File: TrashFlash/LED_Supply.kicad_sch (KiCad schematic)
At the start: 17 parts, among them IC1 LTC3643IUDD#PBF

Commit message: Added Power Supply
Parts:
- R14: value 3.3M -> 560k
- R15: value 68k -> 12k
- R17: value 470k -> 56k
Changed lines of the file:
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@@
 			)
 		)
-		(property "Value" "68k"
+		(property "Value" "12k"
 			(at 160.02 93.9799 0)
 			(effects
@@
 			)
 		)
-		(property "Value" "3.3M"
+		(property "Value" "560k"
 			(at 160.02 69.8499 0)
 			(effects
@@
 			)
 		)
-		(property "Value" "470k"
+		(property "Value" "56k"
 			(at 125.73 83.82 90)
 			(effects

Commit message: Added Battery Management
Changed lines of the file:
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@@
 	)
 	(hierarchical_label "V_LED"
-		(shape input)
+		(shape output)
 		(at 222.25 63.5 0)
 		(effects

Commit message: Added USB and powernets
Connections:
- net V_BAT renamed VSYS
- net V_LED renamed Vdrive
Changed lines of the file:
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@@
+	(wire
+		(pts
+			(xy 55.88 38.1) (xy 93.98 38.1)
+		)
+		(stroke
+			(width 0)
+			(type default)
+		)
+	)
 	(wire
 		(pts
@@
 	(wire
 		(pts
-			(xy 195.58 63.5) (xy 222.25 63.5)
-		)
-		(stroke
-			(width 0)
-			(type default)
-		)
-	)
-	(wire
-		(pts
 			(xy 157.48 87.63) (xy 157.48 88.9)
 		)
@@
 	(wire
 		(pts
-			(xy 54.61 38.1) (xy 93.98 38.1)
-		)
-		(stroke
-			(width 0)
-			(type default)
-		)
-	)
-	(wire
-		(pts
 			(xy 157.48 120.65) (xy 157.48 121.92)
 		)
@@
 	(wire
 		(pts
+			(xy 195.58 59.69) (xy 195.58 63.5)
+		)
+		(stroke
+			(width 0)
+			(type default)
+		)
+	)
+	(wire
+		(pts
 			(xy 93.98 63.5) (xy 93.98 64.77)
 		)
@@
 			(width 0)
 			(type default)
-		)
-	)
-	(hierarchical_label "V_BAT"
-		(shape input)
-		(at 54.61 38.1 180)
-		(effects
-			(font
-				(size 1.27 1.27)
-			)
-			(justify right)
-		)
-	)
-	(hierarchical_label "V_LED"
-		(shape output)
-		(at 222.25 63.5 0)
-		(effects
-			(font
-				(size 1.27 1.27)
-			)
-			(justify left)
 		)
 	)
@@
 	)
 	(symbol
+		(lib_id "TrashFlash:VSYS")
+		(at 55.88 38.1 90)
+		(unit 1)
+		(exclude_from_sim no)
+		(in_bom yes)
+		(on_board yes)
+		(dnp no)
+		(fields_autoplaced yes)
+		(property "Reference" "#PWR051"
+			(at 50.292 27.94 0)
+			(effects
+				(font
+					(size 1.27 1.27)
+				)
+				(hide yes)
+			)
+		)
+		(property "Value" "VSYS"
+			(at 52.07 38.0999 90)
+			(effects
+				(font
+					(size 1.27 1.27)
+				)
+				(justify left)
+			)
+		)
+		(property "Footprint" ""
+			(at 55.88 38.1 0)
+			(effects
+				(font
+					(size 1.27 1.27)
+				)
+				(hide yes)
+			)
+		)
+		(property "Datasheet" ""
+			(at 55.88 38.1 0)
+			(effects
+				(font
+					(size 1.27 1.27)
+				)
+				(hide yes)
+			)
+		)
+		(property "Description" "Power symbol creates a global label with name \"VSYS\""
+			(at 46.482 37.592 0)
+			(effects
+				(font
+					(size 1.27 1.27)
+				)
+				(hide yes)
+			)
+		)
+		(pin "1"
+		)
+		(instances
+			(project ""
+				(path "/256082dc-9c82-41ae-bfb7-0b4bd4121c78/20812885-5a6f-4708-82f0-e6ad3403d690"
+					(reference "#PWR051")
+					(unit 1)
+				)
+			)
+		)
+	)
+	(symbol
 		(lib_id "power:GND")
 		(at 195.58 143.51 0)
@@
 				)
 			)
+		)
+	)
+	(symbol
+		(lib_id "power:Vdrive")
+		(at 195.58 59.69 0)
+		(unit 1)
+		(exclude_from_sim no)
+		(in_bom yes)
+		(on_board yes)
+		(dnp no)
+		(fields_autoplaced yes)
+		(property "Reference" "#PWR050"
+			(at 195.58 63.5 0)
+			(effects
+				(font
+					(size 1.27 1.27)
+				)
+				(hide yes)
+			)
+		)
+		(property "Value" "Vdrive"
+			(at 195.58 54.61 0)
+			(effects
+				(font
+					(size 1.27 1.27)
+				)
+			)
+		)
+		(property "Footprint" ""
+			(at 195.58 59.69 0)
+			(effects
+				(font
+					(size 1.27 1.27)
+				)
+				(hide yes)
+			)
+		)
+		(property "Datasheet" ""
+			(at 195.58 59.69 0)
+			(effects
+				(font
+					(size 1.27 1.27)
+				)
+				(hide yes)
+			)
+		)
+		(property "Description" "Power symbol creates a global label with name \"Vdrive\""
+			(at 195.58 59.69 0)
+			(effects
+				(font
+					(size 1.27 1.27)
+				)
+				(hide yes)
+			)
+		)
+		(pin "1"
+		)
+		(instances
+			(project ""
+				(path "/256082dc-9c82-41ae-bfb7-0b4bd4121c78/20812885-5a6f-4708-82f0-e6ad3403d690"
+					(reference "#PWR050")
+					(unit 1)
+				)
+			)

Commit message: Rotary encoder added + 3D stuff
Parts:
- C10, C6, C9: footprint (none) -> Capacitor_SMD:C_0402_1005Metric
- C11, C5, C7: footprint (none) -> Capacitor_SMD:C_0603_1608Metric
- IC1: footprint QFN50P300X500X80-25N-D -> TrashFlash:QFN50P300X500X80-25N-D
- L1: footprint INDPM5454X310N -> TrashFlash:INDPM5454X310N
- R10: footprint (none) -> Resistor_SMD:R_0603_1608Metric
- R11, R12, R13, R14, R15, R16, R17: footprint (none) -> Resistor_SMD:R_0402_1005Metric
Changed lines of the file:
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@@
 			)
 		)
-		(property "Footprint" ""
+		(property "Footprint" "Resistor_SMD:R_0402_1005Metric"
 			(at 159.258 92.71 90)
 			(effects
@@
 			)
 		)
-		(property "Footprint" ""
+		(property "Footprint" "Resistor_SMD:R_0402_1005Metric"
 			(at 159.258 68.58 90)
 			(effects
@@
 			)
 		)
-		(property "Footprint" ""
+		(property "Footprint" "Capacitor_SMD:C_0402_1005Metric"
 			(at 158.4452 129.54 0)
 			(effects
@@
 			)
 		)
-		(property "Footprint" ""
+		(property "Footprint" "Capacitor_SMD:C_0603_1608Metric"
 			(at 75.8952 36.83 0)
 			(effects
@@
 			)
 		)
-		(property "Footprint" ""
+		(property "Footprint" "Capacitor_SMD:C_0603_1608Metric"
 			(at 196.5452 129.54 0)
 			(effects
@@
 			)
 		)
-		(property "Footprint" ""
+		(property "Footprint" "Resistor_SMD:R_0402_1005Metric"
 			(at 95.758 58.42 90)
 			(effects
@@
 			)
 		)
-		(property "Footprint" ""
+		(property "Footprint" "Resistor_SMD:R_0402_1005Metric"
 			(at 95.758 48.26 90)
 			(effects
@@
 			)
 		)
-		(property "Footprint" ""
+		(property "Footprint" "Capacitor_SMD:C_0603_1608Metric"
 			(at 177.4952 72.39 0)
 			(effects
@@
 			)
 		)
-		(property "Footprint" ""
+		(property "Footprint" "Resistor_SMD:R_0603_1608Metric"
 			(at 95.758 33.02 90)
 			(effects
@@
 			)
 		)
-		(property "Footprint" ""
+		(property "Footprint" "Resistor_SMD:R_0402_1005Metric"
 			(at 125.73 85.852 90)
 			(effects
@@
 			)
 		)
-		(property "Footprint" "QFN50P300X500X80-25N-D"
+		(property "Footprint" "TrashFlash:QFN50P300X500X80-25N-D"
 			(at 113.284 170.434 0)
 			(effects
@@
 			)
 		)
-		(property "Footprint" "INDPM5454X310N"
+		(property "Footprint" "TrashFlash:INDPM5454X310N"
 			(at 173.99 129.21 0)
 			(effects
@@
 			)
 		)
-		(property "Footprint" "QFN50P300X500X80-25N-D"
+		(property "Footprint" "TrashFlash:QFN50P300X500X80-25N-D"
 			(at 113.284 80.264 0)
 			(effects
@@
 			)
 		)
-		(property "Footprint" ""
+		(property "Footprint" "Capacitor_SMD:C_0402_1005Metric"
 			(at 177.4952 129.54 0)
 			(effects
@@
 			)
 		)
-		(property "Footprint" ""
+		(property "Footprint" "Capacitor_SMD:C_0402_1005Metric"
 			(at 158.4452 52.07 0)
 			(effects
@@
 			)
 		)
-		(property "Footprint" ""
+		(property "Footprint" "Resistor_SMD:R_0402_1005Metric"
 			(at 95.758 68.58 90)
 			(effects
@@
 			)
 		)
-		(property "Footprint" ""
+		(property "Footprint" "Resistor_SMD:R_0402_1005Metric"
 			(at 159.258 135.89 90)
 			(effects

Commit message: Footprints 3D model fixed
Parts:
- IC1: footprint TrashFlash:QFN50P300X500X80-25N-D -> QFN50P300X500X80-25N-D
- L1: footprint TrashFlash:INDPM5454X310N -> INDPM5454X310N
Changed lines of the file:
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@@
 	)
 	(symbol
-		(lib_name "LTC3643IUDD#PBF_1")
 		(lib_id "TrashFlash:LTC3643IUDD#PBF")
 		(at 125.73 113.03 0)
@@
 			)
 		)
-		(property "Footprint" "TrashFlash:QFN50P300X500X80-25N-D"
+		(property "Footprint" "QFN50P300X500X80-25N-D"
 			(at 113.284 170.434 0)
 			(effects
@@
 			)
 		)
-		(property "Footprint" "TrashFlash:INDPM5454X310N"
+		(property "Footprint" "INDPM5454X310N"
 			(at 173.99 129.21 0)
 			(effects
@@
 			)
 		)
-		(property "Footprint" "TrashFlash:QFN50P300X500X80-25N-D"
+		(property "Footprint" "QFN50P300X500X80-25N-D"
 			(at 113.284 80.264 0)
 			(effects

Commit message: Added STM32 to schematic
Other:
- note added: "Change this so we can turn on with MCU!"
- note added: "Vdrive range: 16.6 V to 34.6 V"
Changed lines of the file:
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@@
 	(generator_version "9.0")
 	(paper "A4")
+	(text "Vdrive range:\n16.6 V to 34.6 V"
+		(exclude_from_sim no)
+		(at 144.78 85.09 0)
+		(effects
+			(font
+				(face "Consolas")
+				(size 1.27 1.27)
+			)
+		)
+	)
+	(text "Change this so we can turn on with MCU!\n"
+		(exclude_from_sim no)
+		(at 90.678 60.706 90)
+		(effects
+			(font
+				(face "Consolas")
+				(size 1.27 1.27)
+			)
+		)
+	)
 	(junction
 		(at 176.53 63.5)

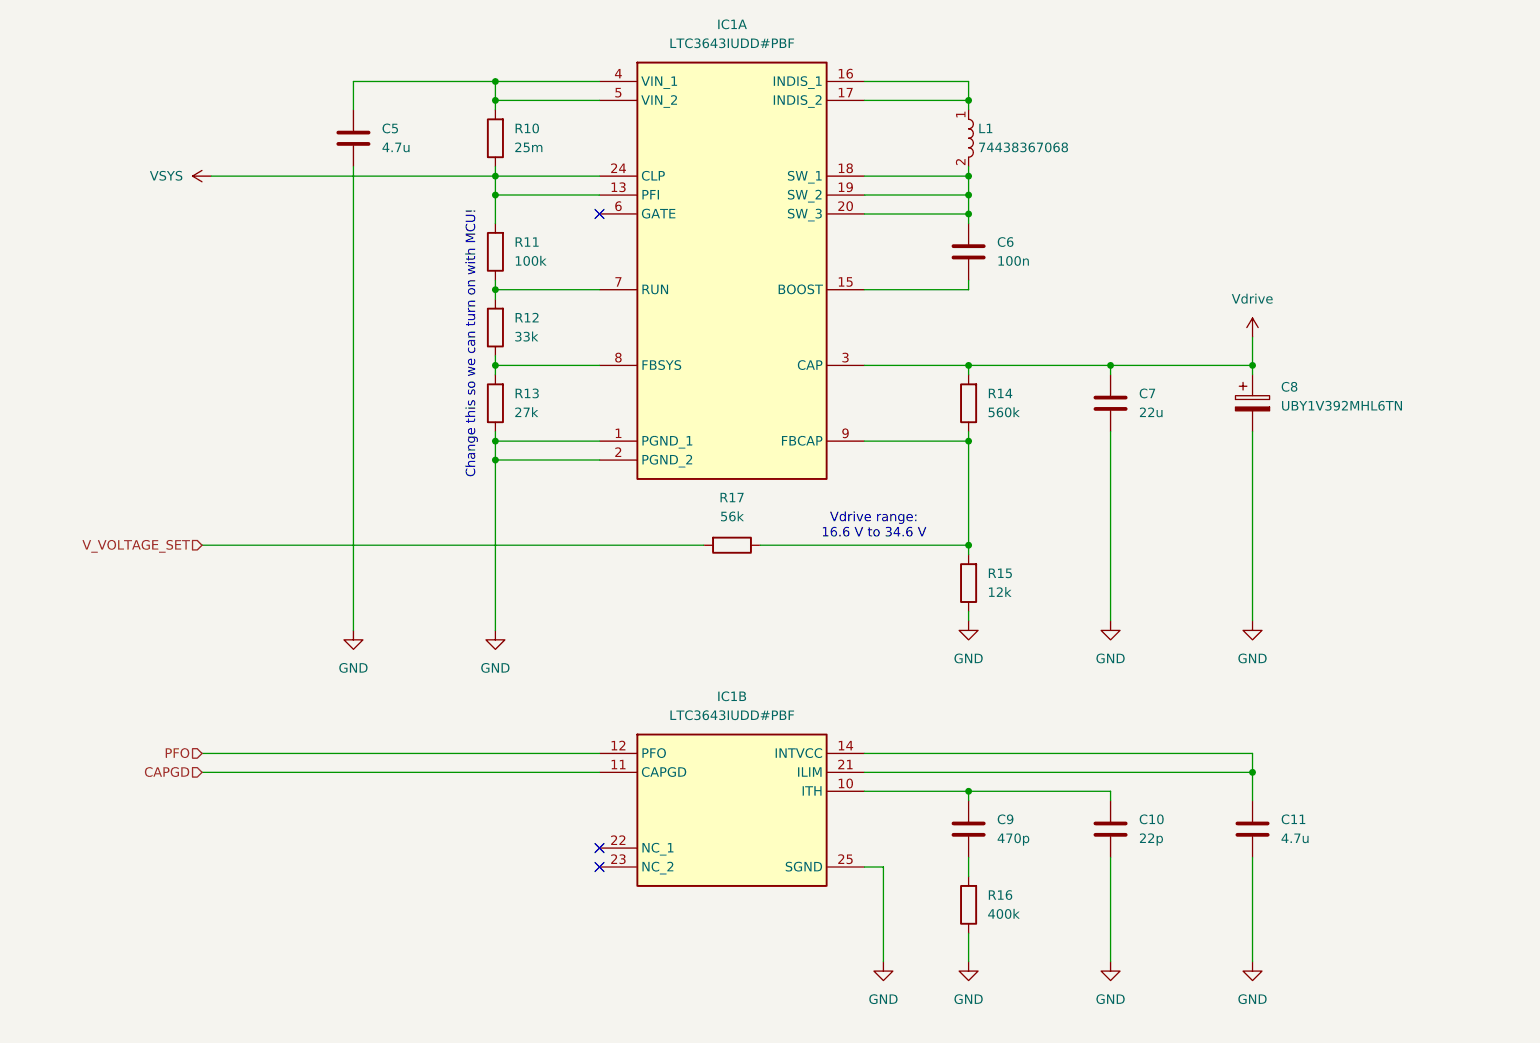
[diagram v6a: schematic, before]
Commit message: Added netlabels / cleaned up schematic
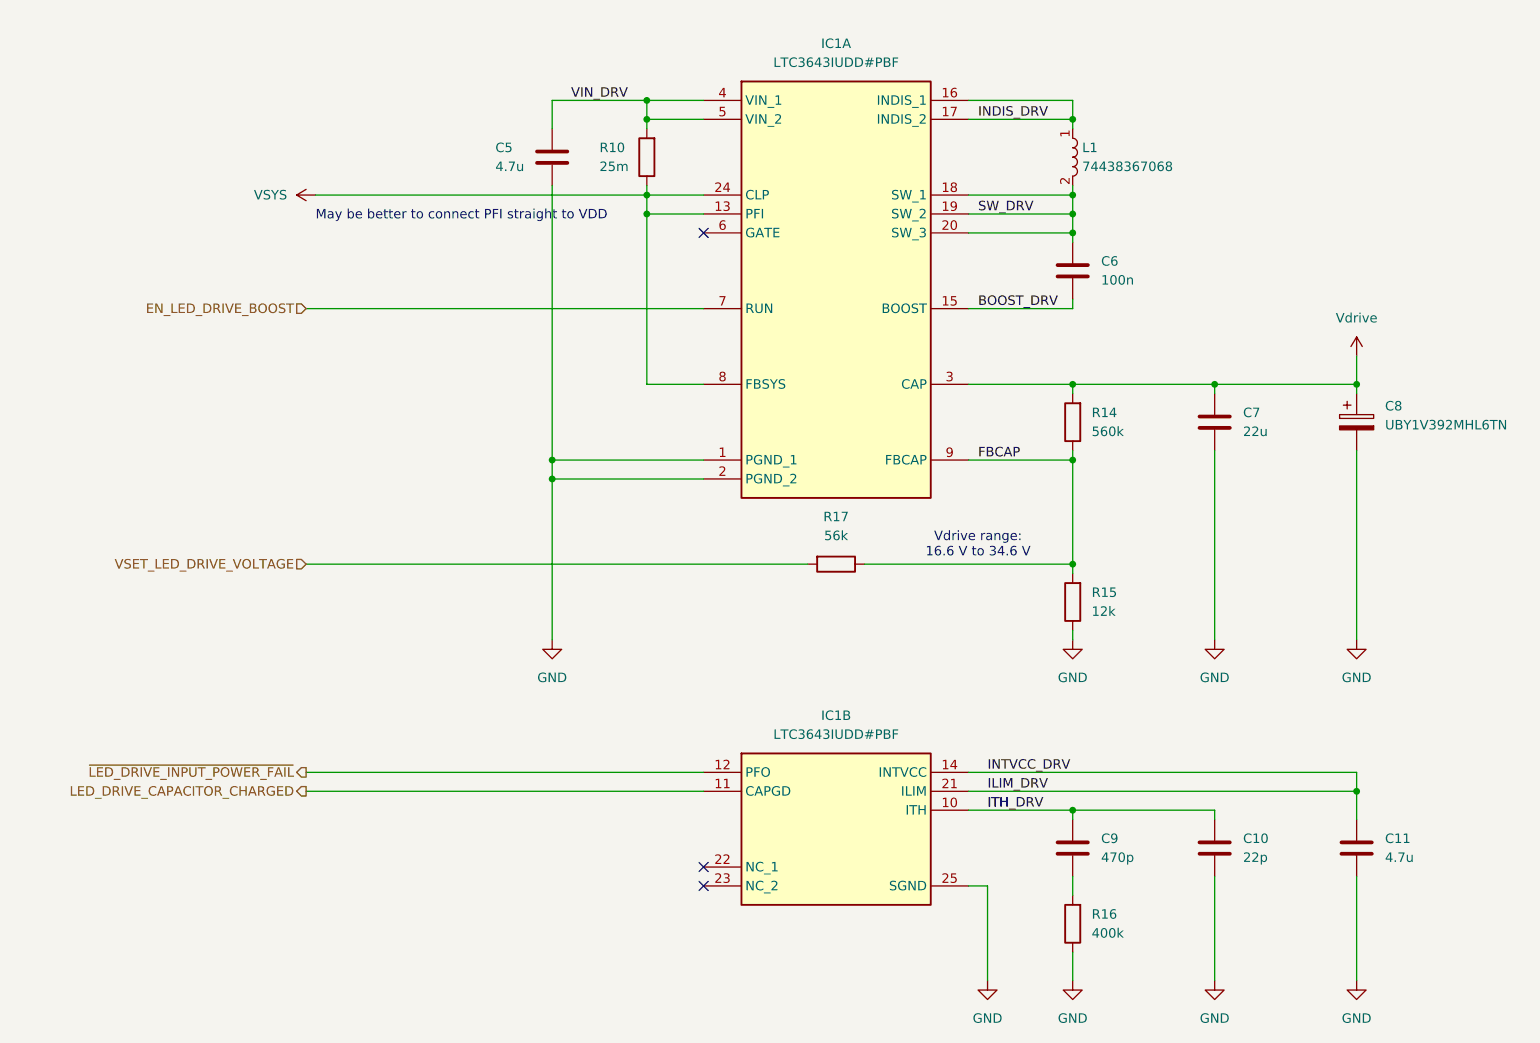
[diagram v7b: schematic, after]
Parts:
- removed R11: 100k, Resistor_SMD:R_0402_1005Metric, symbol Device:R
- removed R12: 33k, Resistor_SMD:R_0402_1005Metric, symbol Device:R
- removed R13: 27k, Resistor_SMD:R_0402_1005Metric, symbol Device:R
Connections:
- net VSYS: now also IC1.8 (FBSYS)
- net FBCAP: now reaches IC1.9 (FBCAP), R14.1, R15.2, R17.1
- net ITH: now reaches C10.1, C9.1, IC1.10 (ITH)
- net VIN_DRV: now reaches C5.1, IC1.4 (VIN_1), IC1.5 (VIN_2), R10.2
- net ILIM_DRV: now reaches C11.1, IC1.14 (INTVCC), IC1.21 (ILIM)
- net EN_LED_DRIVE_BOOST: now reaches IC1.7 (RUN)
- net INDIS_DRV: now reaches IC1.16 (INDIS_1), IC1.17 (INDIS_2), L1.1
- net SW_DRV: now reaches C6.1, IC1.18 (SW_1), IC1.19 (SW_2), IC1.20 (SW_3), L1.2
- net BOOST_DRV: now reaches C6.2, IC1.15 (BOOST)
- net CAPGD renamed LED_DRIVE_CAPACITOR_CHARGED
- net PFO renamed ~{LED_DRIVE_INPUT_POWER_FAIL}
- net V_VOLTAGE_SET renamed VSET_LED_DRIVE_VOLTAGE
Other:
- note added: "May be better to connect PFI straight to VDD"
- note removed: "Change this so we can turn on with MCU!"
- moved on the sheet: C10, C11, C5, C6, C7, C8, C9, IC1A, IC1B, L1, R10, R14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

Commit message: Added 3D-models to footprints, PCB outline and component placement
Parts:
- IC1: footprint QFN50P300X500X80-25N-D -> TrashFlash:QFN50P300X500X80-25N-D
- L1: footprint INDPM5454X310N -> TrashFlash:INDPM5454X310N
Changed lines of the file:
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@@
 			)
 		)
-		(property "Footprint" "QFN50P300X500X80-25N-D"
+		(property "Footprint" "TrashFlash:QFN50P300X500X80-25N-D"
 			(at 127.254 172.974 0)
 			(effects
@@
 			)
 		)
-		(property "Footprint" "INDPM5454X310N"
+		(property "Footprint" "TrashFlash:INDPM5454X310N"
 			(at 187.96 131.75 0)
 			(effects
@@
 			)
 		)
-		(property "Footprint" "QFN50P300X500X80-25N-D"
+		(property "Footprint" "TrashFlash:QFN50P300X500X80-25N-D"
 			(at 127.254 82.804 0)
 			(effects
